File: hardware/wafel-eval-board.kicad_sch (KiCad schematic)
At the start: 46 parts, among them Q101 AO3422, U101 LM5163DDA

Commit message: improve can
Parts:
- added J101: CAN PORT, Connector_JST:JST_PH_S4B-PH-K_1x04_P2.00mm_Horizontal, symbol Connector:Conn_01x04_Pin
- added J102: SW, Connector_JST:JST_PH_S2B-PH-K_1x02_P2.00mm_Horizontal, symbol Connector:Conn_01x02_Pin
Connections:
- new net CAN.H: J101.2 (Pin_2)
- new net CAN.L: J101.3 (Pin_3)
- new net VESC.GND: J102.1 (Pin_1)
- new net VESC.SW: J102.2 (Pin_2)
- no-connect marks 1 -> 3
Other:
- moved on the sheet: H113, H114, H115

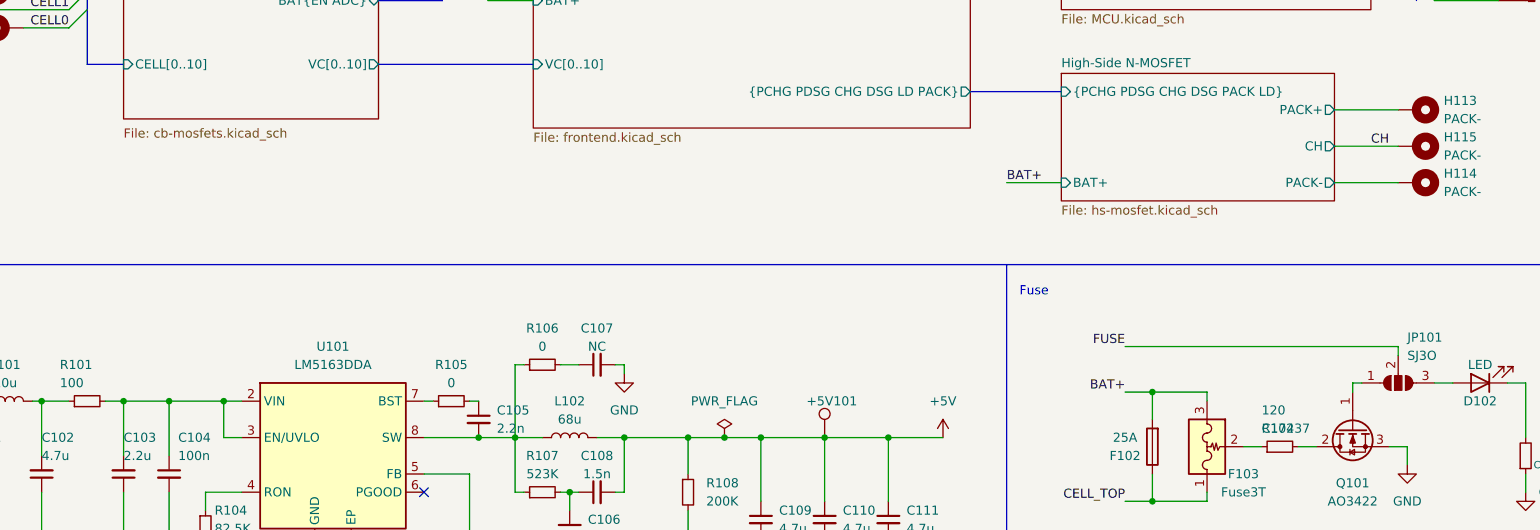
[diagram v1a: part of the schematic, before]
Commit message: fix MCU pin mapping and resolve ERC conflicts
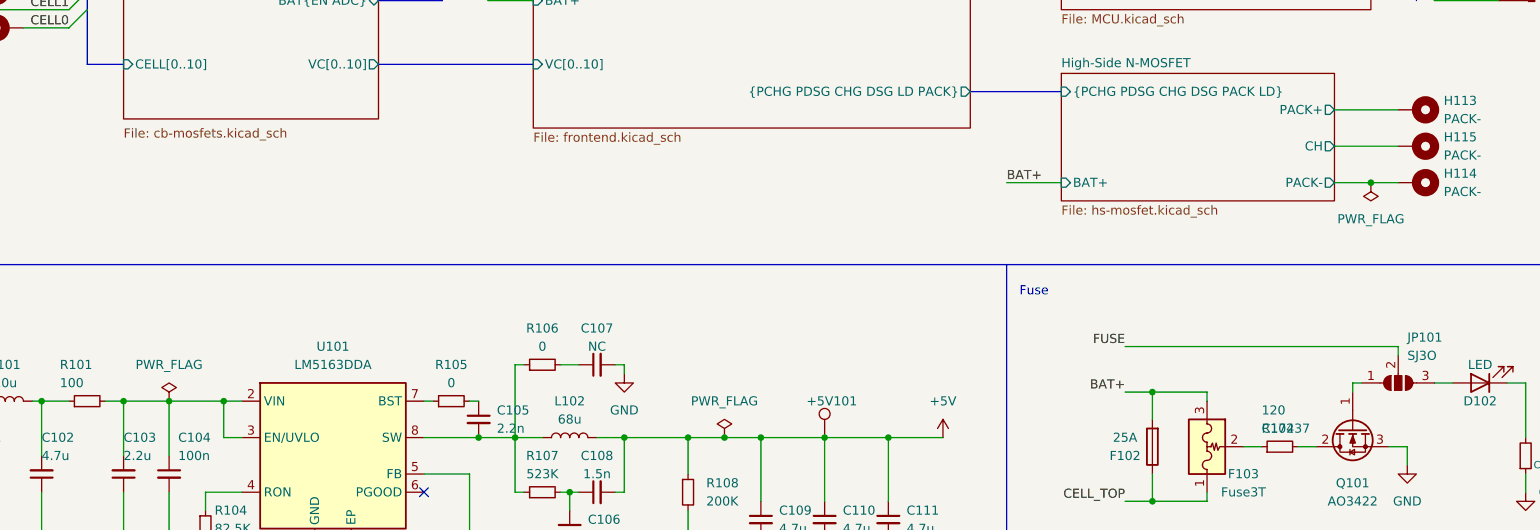
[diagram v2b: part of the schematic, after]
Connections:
- net CH renamed High-Side N-MOSFET/CH
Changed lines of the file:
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@@
 	)
 	(junction
+		(at 238.76 97.79)
+		(diameter 0)
+		(color 0 0 0 0)
+	)
+	(junction
 		(at 162.56 133.35)
 		(diameter 0)
@@
 	(wire
 		(pts
-			(xy 233.68 97.79) (xy 242.57 97.79)
+			(xy 233.68 97.79) (xy 238.76 97.79)
+		)
+		(stroke
+			(width 0)
+			(type default)
+		)
+	)
+	(wire
+		(pts
+			(xy 238.76 97.79) (xy 242.57 97.79)
 		)
 		(stroke
@@
 		)
 	)
-	(label "CH"
-		(at 241.3 92.71 180)
-		(effects
-			(font
-				(size 1.27 1.27)
-			)
-			(justify right bottom)
-		)
-	)
 	(label "CELL2"
 		(at 57.15 71.12 180)
@@
 	)
 	(symbol
+		(lib_id "power:PWR_FLAG")
+		(at 238.76 97.79 180)
+		(unit 1)
+		(body_style 1)
+		(exclude_from_sim no)
+		(in_bom yes)
+		(on_board yes)
+		(in_pos_files yes)
+		(dnp no)
+		(fields_autoplaced yes)
+		(property "Reference" "#FLG0103"
+			(at 238.76 99.695 0)
+			(hide yes)
+			(show_name no)
+			(do_not_autoplace no)
+			(effects
+				(font
+					(size 1.27 1.27)
+				)
+			)
+		)
+		(property "Value" "PWR_FLAG"
+			(at 238.76 102.87 0)
+			(show_name no)
+			(do_not_autoplace no)
+			(effects
+				(font
+					(size 1.27 1.27)
+				)
+			)
+		)
+		(property "Footprint" ""
+			(at 238.76 97.79 0)
+			(hide yes)
+			(show_name no)
+			(do_not_autoplace no)
+			(effects
+				(font
+					(size 1.27 1.27)
+				)
+			)
+		)
+		(property "Datasheet" ""
+			(at 238.76 97.79 0)
+			(hide yes)
+			(show_name no)
+			(do_not_autoplace no)
+			(effects
+				(font
+					(size 1.27 1.27)
+				)
+			)
+		)
+		(property "Description" "Special symbol for telling ERC where power comes from"
+			(at 238.76 97.79 0)
+			(hide yes)
+			(show_name no)
+			(do_not_autoplace no)
+			(effects
+				(font
+					(size 1.27 1.27)
+				)
+			)
+		)
+		(pin "1"
+		)
+		(instances
+			(project "wafel-eval-board"
+				(path "/3e668e3e-3e16-4665-a807-4735962c41d3"
+					(reference "#FLG0103")
+					(unit 1)
+				)
+			)
+		)
+	)
+	(symbol
 		(lib_id "Mechanical:MountingHole_Pad")
 		(at 34.29 73.66 90)
@@
 					(unit 1)
 				)
+			)
+		)
+	)
+	(symbol
+		(lib_id "power:PWR_FLAG")
+		(at 71.12 128.27 0)
+		(unit 1)
+		(body_style 1)
+		(exclude_from_sim no)
+		(in_bom yes)
+		(on_board yes)
+		(in_pos_files yes)
+		(dnp no)
+		(fields_autoplaced yes)
+		(property "Reference" "#FLG0102"
+			(at 71.12 126.365 0)
+			(hide yes)
+			(show_name no)
+			(do_not_autoplace no)
+			(effects
+				(font
+					(size 1.27 1.27)
+				)
+			)
+		)
+		(property "Value" "PWR_FLAG"
+			(at 71.12 123.19 0)
+			(show_name no)
+			(do_not_autoplace no)
+			(effects
+				(font
+					(size 1.27 1.27)
+				)
+			)
+		)
+		(property "Footprint" ""
+			(at 71.12 128.27 0)
+			(hide yes)
+			(show_name no)
+			(do_not_autoplace no)
+			(effects
+				(font
+					(size 1.27 1.27)
+				)
+			)
+		)
+		(property "Datasheet" ""
+			(at 71.12 128.27 0)
+			(hide yes)
+			(show_name no)
+			(do_not_autoplace no)
+			(effects
+				(font
+					(size 1.27 1.27)
+				)
+			)
+		)
+		(property "Description" "Special symbol for telling ERC where power comes from"
+			(at 71.12 128.27 0)
+			(hide yes)
+			(show_name no)
+			(do_not_autoplace no)
+			(effects
+				(font
+					(size 1.27 1.27)
+				)
+			)
+		)
+		(pin "1"
+		)
+		(instances
+			(project "wafel-eval-board"
+				(path "/3e668e3e-3e16-4665-a807-4735962c41d3"
+					(reference "#FLG0102")
+					(unit 1)
+				)

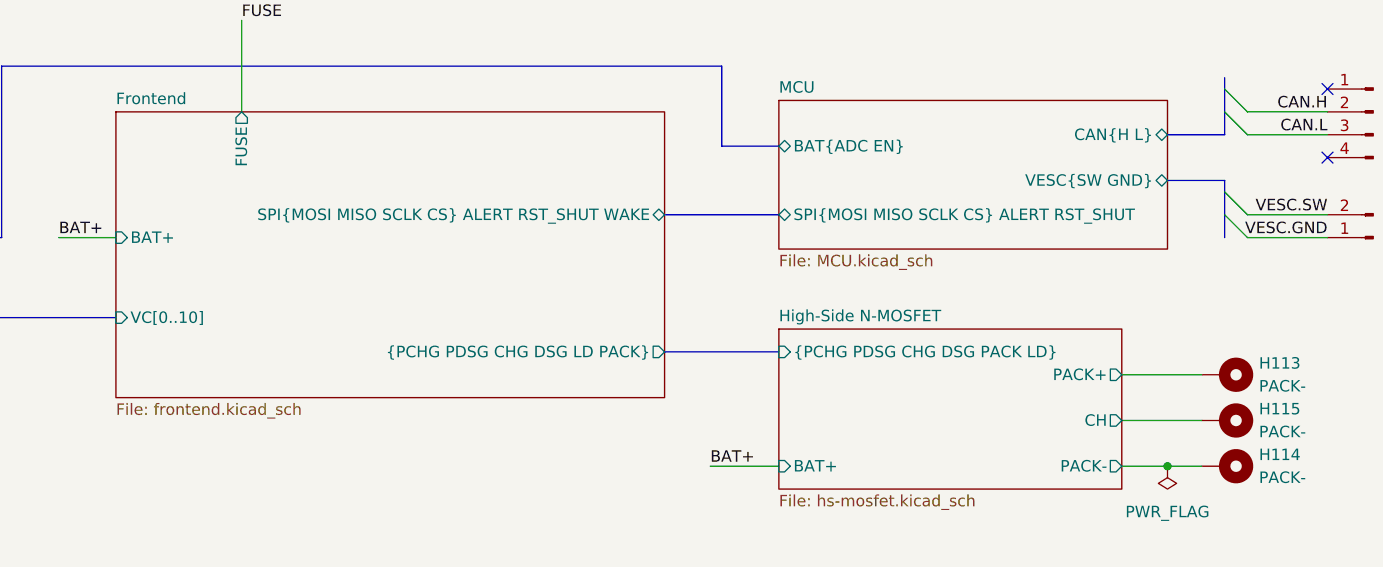
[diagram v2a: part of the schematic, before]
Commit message: use bus alias
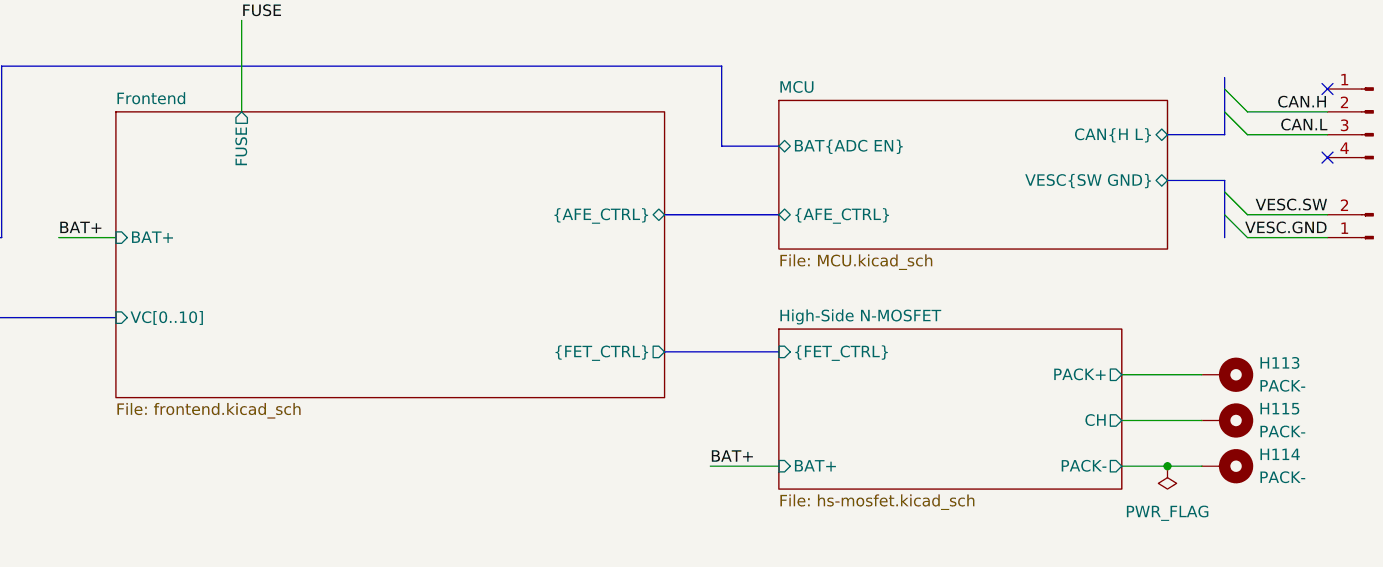
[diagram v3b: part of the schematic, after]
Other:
- sheet Frontend ports: added {AFE_CTRL}, {FET_CTRL}; removed SPI{MOSI MISO SCLK CS} ALERT RST_SHUT WAKE, {PCHG PDSG CHG DSG LD PACK}
- sheet High-Side N-MOSFET ports: added {FET_CTRL}; removed {PCHG PDSG CHG DSG PACK LD}
- sheet MCU ports: added {AFE_CTRL}; removed SPI{MOSI MISO SCLK CS} ALERT RST_SHUT
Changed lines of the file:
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@@
 			)
 		)
-		(pin "{PCHG PDSG CHG DSG LD PACK}" output
+		(pin "{FET_CTRL}" output
 			(at 182.88 85.09 0)
 			(effects
@@
 			)
 		)
-		(pin "SPI{MOSI MISO SCLK CS} ALERT RST_SHUT WAKE" bidirectional
-			(at 182.88 69.85 0)
-			(effects
-				(font
-					(size 1.27 1.27)
-				)
-				(justify right)
-			)
-		)
 		(pin "VC[0..10]" input
 			(at 121.92 81.28 180)
@@
 				)
 				(justify left)
+			)
+		)
+		(pin "{AFE_CTRL}" bidirectional
+			(at 182.88 69.85 0)
+			(effects
+				(font
+					(size 1.27 1.27)
+				)
+				(justify right)
 			)
 		)
@@
 			)
 		)
-		(pin "{PCHG PDSG CHG DSG PACK LD}" input
+		(pin "{FET_CTRL}" input
 			(at 195.58 85.09 180)
 			(effects
@@
 			)
 		)
-		(pin "SPI{MOSI MISO SCLK CS} ALERT RST_SHUT" bidirectional
-			(at 195.58 69.85 180)
-			(effects
-				(font
-					(size 1.27 1.27)
-				)
-				(justify left)
-			)
-		)
 		(pin "BAT{ADC EN}" bidirectional
 			(at 195.58 62.23 180)
@@
 			)
 		)
+		(pin "{AFE_CTRL}" bidirectional
+			(at 195.58 69.85 180)
+			(effects
+				(font
+					(size 1.27 1.27)
+				)
+				(justify left)
+			)
+		)

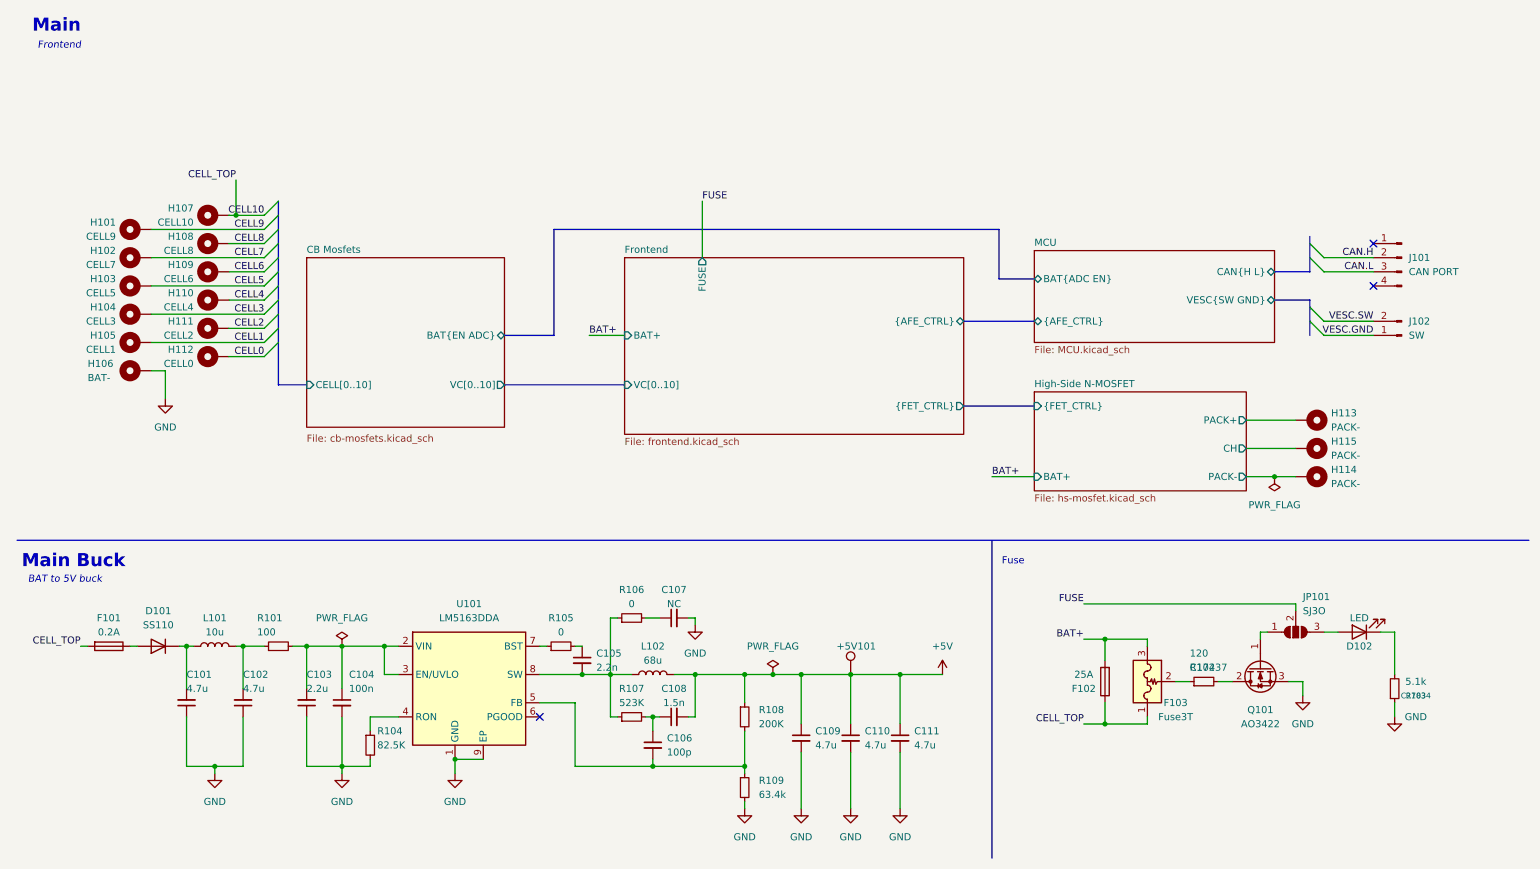
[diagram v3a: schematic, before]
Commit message: fix ERC warnings and footprint issues
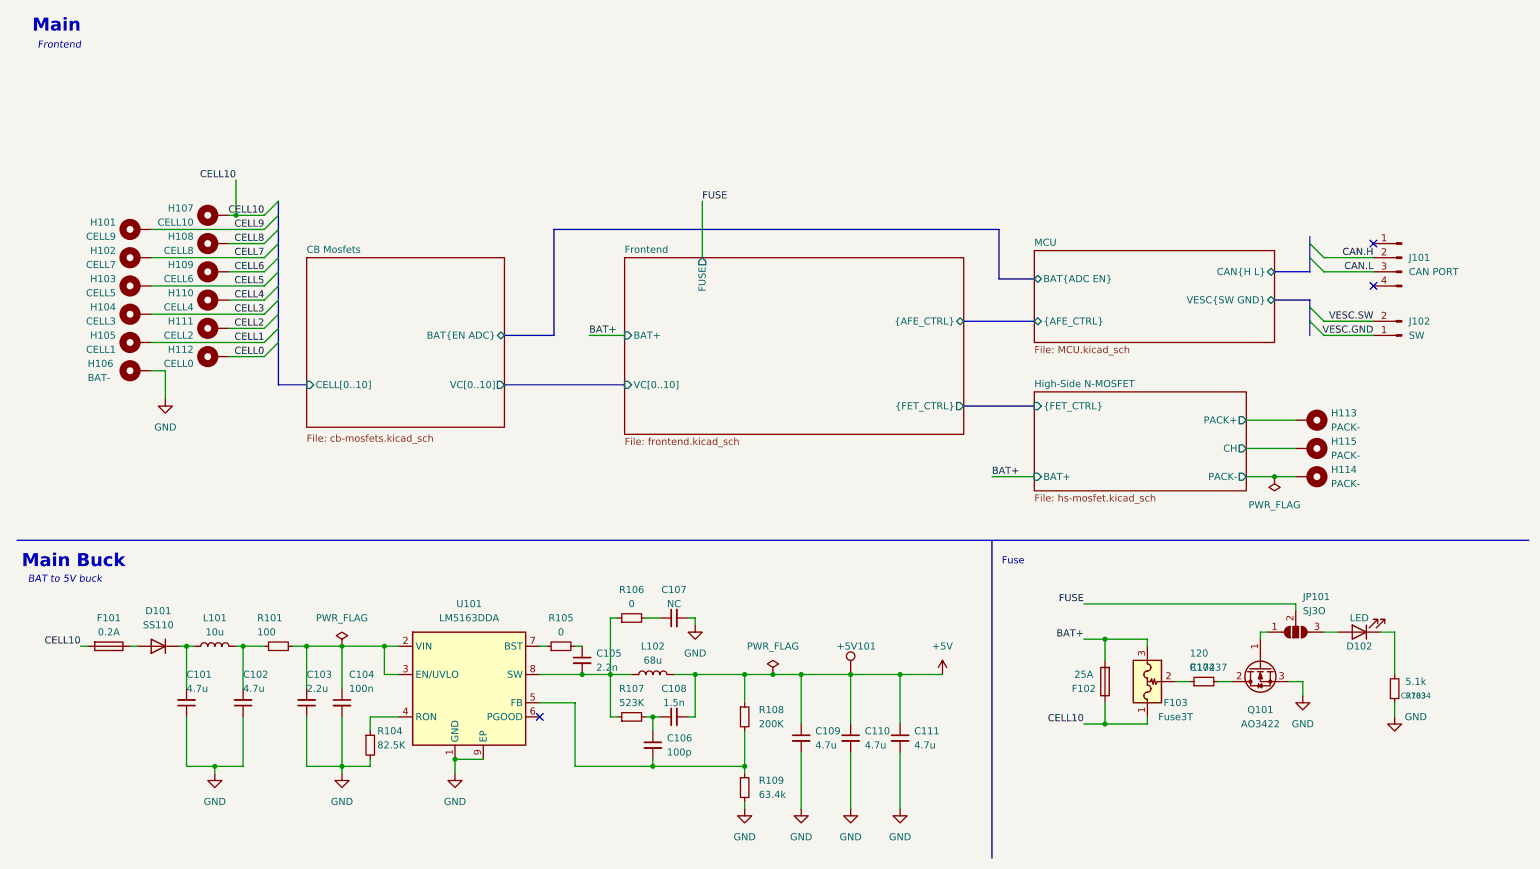
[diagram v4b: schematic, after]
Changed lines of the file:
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@@
 		)
 	)
-	(label "CELL_TOP"
+	(label "CELL10"
 		(at 204.47 142.24 180)
 		(effects
@@
 		)
 	)
-	(label "CELL_TOP"
+	(label "CELL10"
 		(at 52.07 44.45 180)
 		(effects
@@
 		)
 	)
-	(label "CELL_TOP"
+	(label "CELL10"
 		(at 24.13 128.27 180)
 		(effects

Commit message: update schematics
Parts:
- H113: value PACK- -> PACK+
- H115: value PACK- -> CH
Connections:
- net High-Side N-MOSFET/CH renamed CH
- net High-Side N-MOSFET/PACK+ renamed PACK+
- net High-Side N-MOSFET/PACK- renamed PGND
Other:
- sheet High-Side N-MOSFET ports: added none; removed PACK-
- moved on the sheet: H113, H114, H115, J101, J102

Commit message: update schematics
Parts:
- added R110, R111: 2m, Resistor_SMD:R_0805_2012Metric, symbol Device:R_Small
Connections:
- net GND: now also R110.1, R111.1
- net PGND: now also R110.2, R111.2
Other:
- sheet Frontend ports: added BAT-, PACK-; removed none
